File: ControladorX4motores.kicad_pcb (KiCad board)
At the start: 2 copper layers, 120 x 90 mm, 209 parts, among them K1 CONN_3, K2 CONN_3, K3 CONN_3, K4 CONN_3, P1 CONN_6, P10 CONN_4, P11 CONN_4, P12 CONN_4, P13 CONN_2, P2 CONN_6, P3 CONN_6, P4 CONN_6, P9 CONN_4, Q1 BC849, Q10 BC849, Q11 IRF9540N, Q12 IRF540N, Q13 BC849, Q14 BC849, Q15 IRF9540N, Q16 IRF540N, Q17 BC849, Q18 BC849, Q19 IRF9540N, Q2 BC849, Q20 IRF540N, Q21 BC849, Q22 BC849, Q23 IRF9540N, Q24 IRF540N, Q25 BC849, Q26 BC849, Q27 IRF9540N, Q28 IRF540N, Q29 BC849, Q3 IRF9540N, Q30 BC849, Q31 IRF9540N, Q32 IRF540N, Q33 BC849, Q34 BC849, Q35 IRF9540N, Q36 IRF540N, Q37 BC849, Q38 BC849, Q39 IRF9540N, Q4 IRF540N, Q40 IRF540N, Q41 BC849, Q42 BC849, Q43 IRF9540N, Q44 IRF540N, Q45 BC849, Q46 BC849, Q47 IRF9540N, Q48 IRF540N, Q5 BC849, Q6 BC849, Q7 IRF9540N, Q8 IRF540N, Q9 BC849, U1 LM324N, U2 LM324N, U3 LM324N

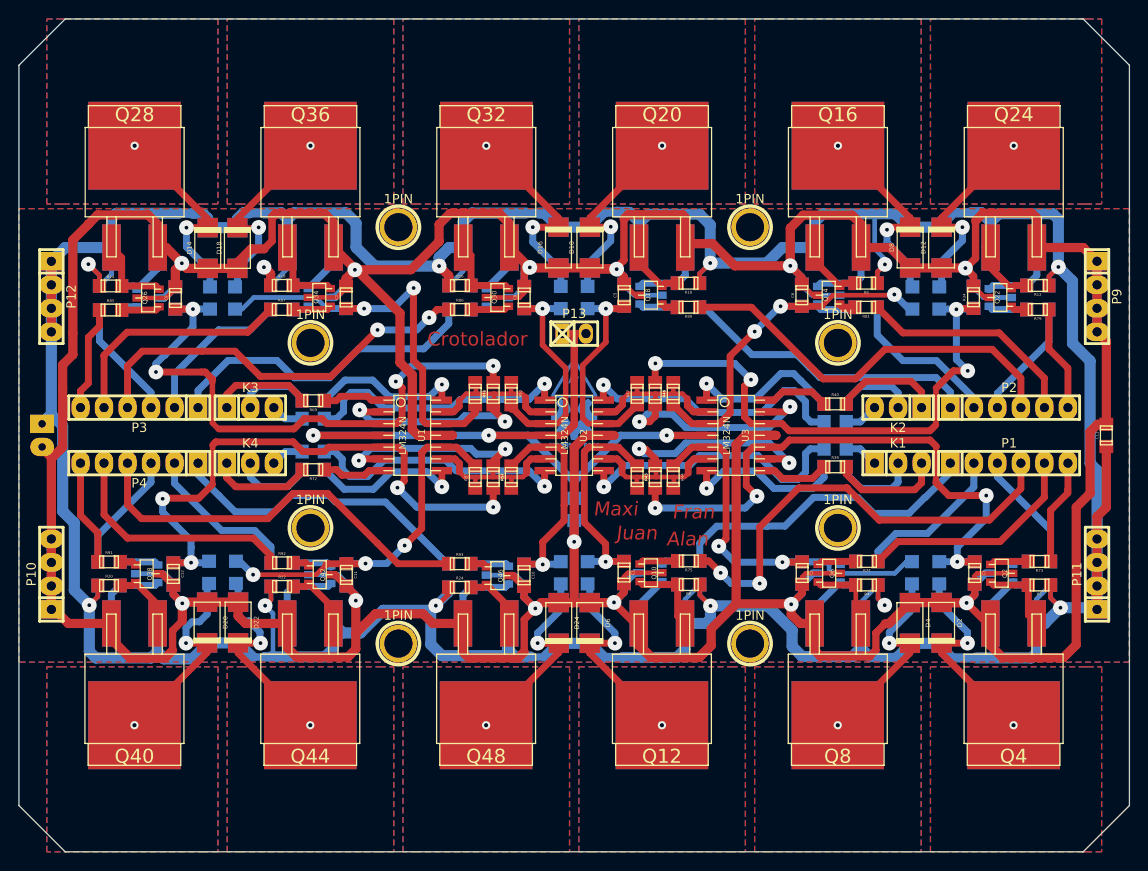
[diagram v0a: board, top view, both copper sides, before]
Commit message: Corregido con agujeros agrandados
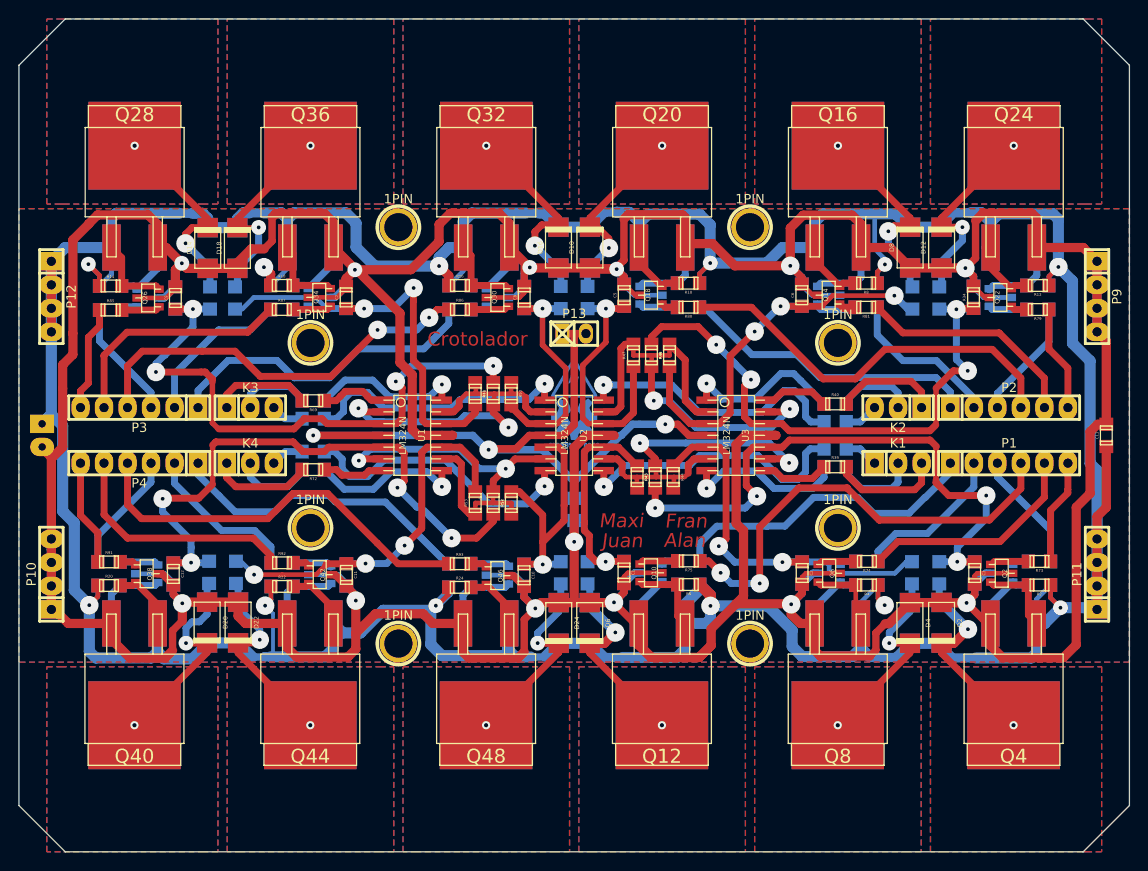
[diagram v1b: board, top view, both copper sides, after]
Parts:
- moved R46 4.17 mm to (158.3, 108.8)
- moved R47 4.17 mm to (156.4, 108.8)
- moved R48 4.17 mm to (160.3, 108.8)
- moved R52 2.80 mm to (143.2, 124.8)
- moved R53 2.80 mm to (139.3, 124.8)
- moved R54 2.80 mm to (141.2, 124.8)
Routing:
- net V_5v: track 126.2 -> 101.3 mm
- net N-0000089: track 41.7 -> 31.1 mm
- net N-0000082: track 43.4 -> 49.5 mm
- net /Detector_Cruce/Fase13: track 38.7 -> 32.8 mm
- net N-0000098: track 44.7 -> 50.3 mm
- net /MOSFET_Potencia1/Fase1: track 38.7 -> 33.2 mm
- net /Detector_Cruce/Fase23: track 38.7 -> 33.2 mm
- net /MOSFET_Potencia4/Fase2: track 38.2 -> 33.1 mm
- net /MOSFET_Potencia3/Fase3: track 36.7 -> 33.1 mm
- net N-00000105: track 41.0 -> 44.2 mm
- net N-00000107: track 51.6 -> 49.8 mm
- net N-0000099: track 29.2 -> 30.8 mm
- net N-0000086: track 30.3 -> 31.6 mm
- net N-0000087: track 78.3 -> 79.5 mm
- net /MOSFET_Potencia2/Fase2: track 33.2 -> 32.1 mm
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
